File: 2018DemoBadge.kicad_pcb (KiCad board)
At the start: 2 copper layers, 8 parts, among them U1 PIC16F15325

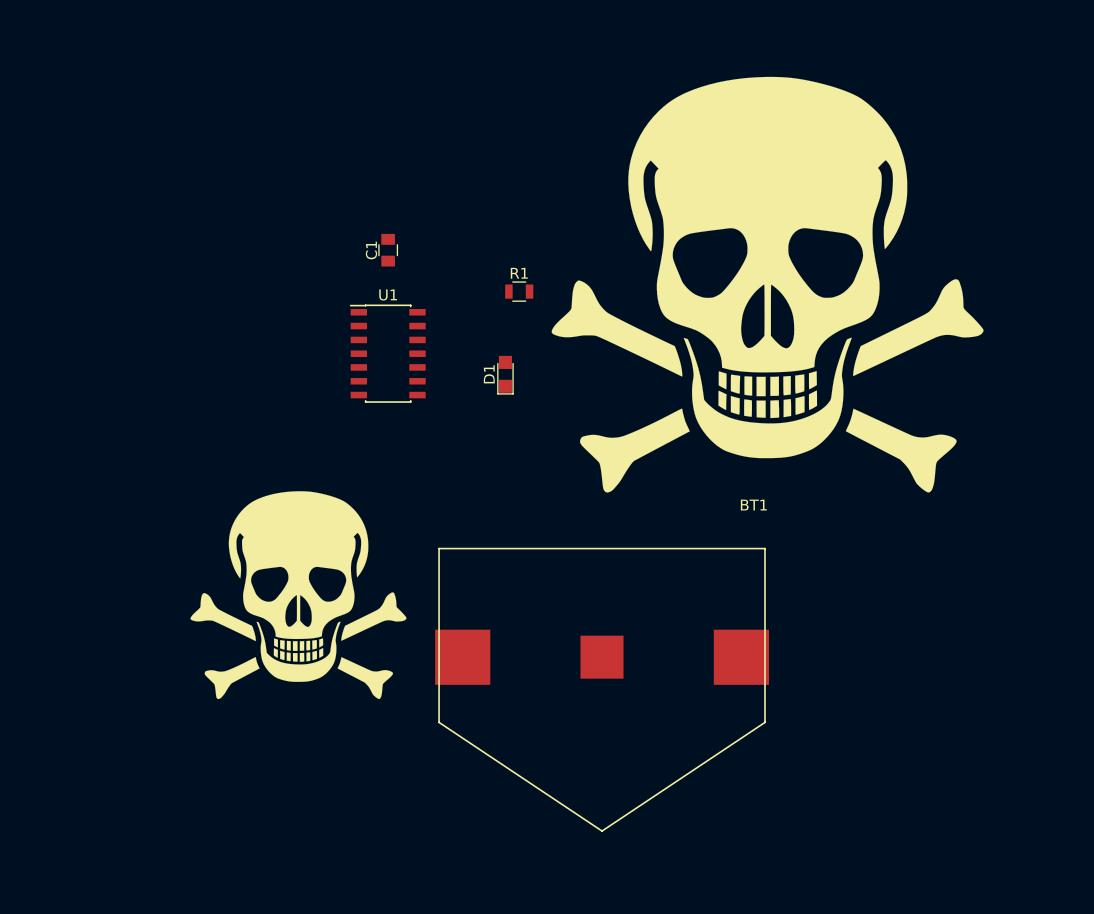
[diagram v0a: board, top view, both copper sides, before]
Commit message: skulls and copper fill zone unconnected
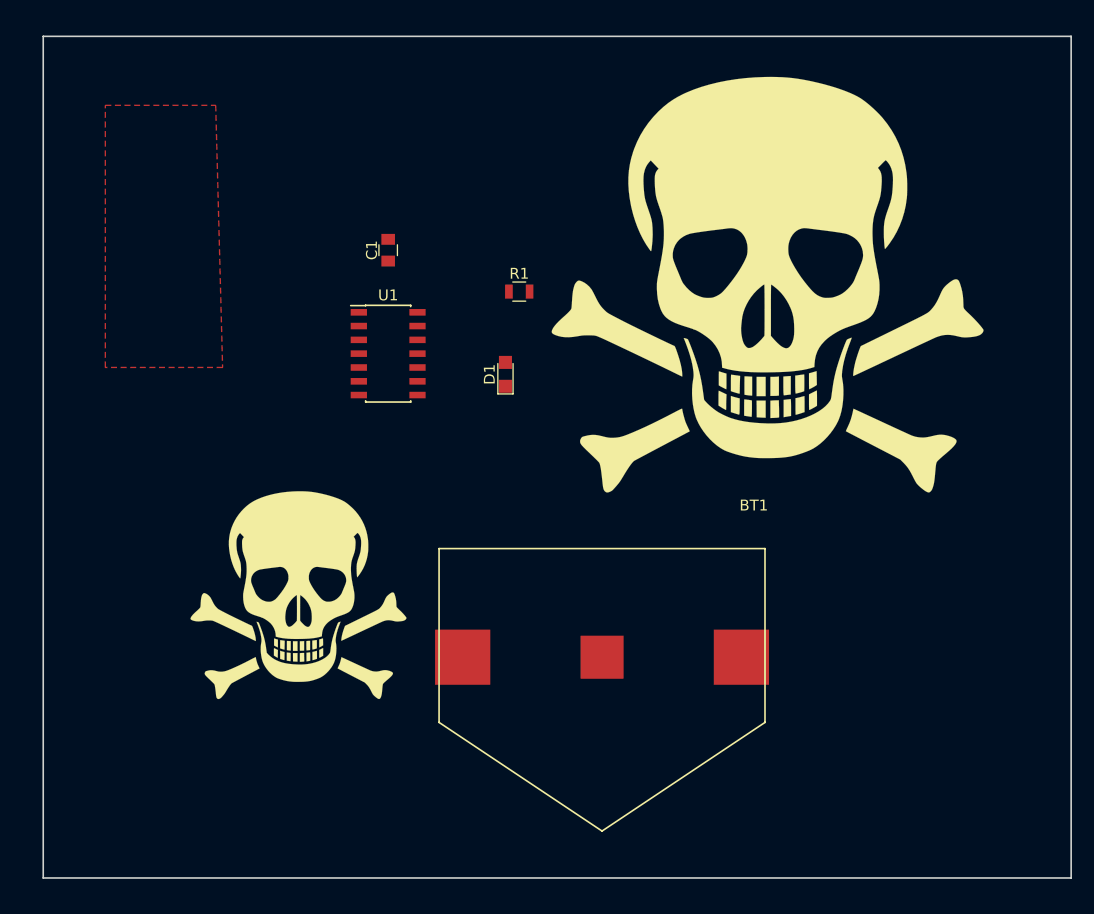
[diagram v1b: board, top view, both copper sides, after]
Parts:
- moved G*** 4.26 mm to (113.7, 87.0)
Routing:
- added copper zone on F.Cu, net (none)
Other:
- board outline added: 94.6 x 77.5 mm
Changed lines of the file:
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@@
     (links 8)
     (no_connects 8)
-    (area 105.430881 70.84252 185.181817 140.735001)
+    (area 98.349999 67.234999 193.115001 144.855001)
     (thickness 1.6)
-    (drawings 0)
+    (drawings 4)
     (tracks 0)
     (zones 0)
@@
   )
   (module FootprintLibrary:SkullCrossbones2000SM (layer F.Cu)
-    (at 115.57 83.185)
+    (at 113.665 86.995)
     (fp_text reference G*** (at 0 0) (layer F.SilkS) hide
       (effects (font (thickness 0.3)))
@@
       (xy 0.432817 -9.558067)) (layer F.Mask) (width 0.01))
   )
+  (gr_line (start 193.04 67.31) (end 98.425 67.31) (angle 90) (layer Edge.Cuts) (width 0.15))
+  (gr_line (start 193.04 144.78) (end 193.04 67.31) (angle 90) (layer Edge.Cuts) (width 0.15))
+  (gr_line (start 98.425 144.78) (end 193.04 144.78) (angle 90) (layer Edge.Cuts) (width 0.15))
+  (gr_line (start 98.425 67.31) (end 98.425 144.78) (angle 90) (layer Edge.Cuts) (width 0.15))
+  (zone (net 0) (net_name "") (layer F.Cu) (hatch edge 0.508)
+    (connect_pads (clearance 0.508))
+    (min_thickness 0.254)
+    (fill yes (arc_segments 16) (thermal_gap 0.508) (thermal_bridge_width 0.508))
+    (polygon
+      (pts
+        (xy 114.935 97.79) (xy 104.14 97.79) (xy 104.14 73.66) (xy 114.3 73.66)
+      )
+    )
+  )
 )

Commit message: skulls and copper fill zone unconnected
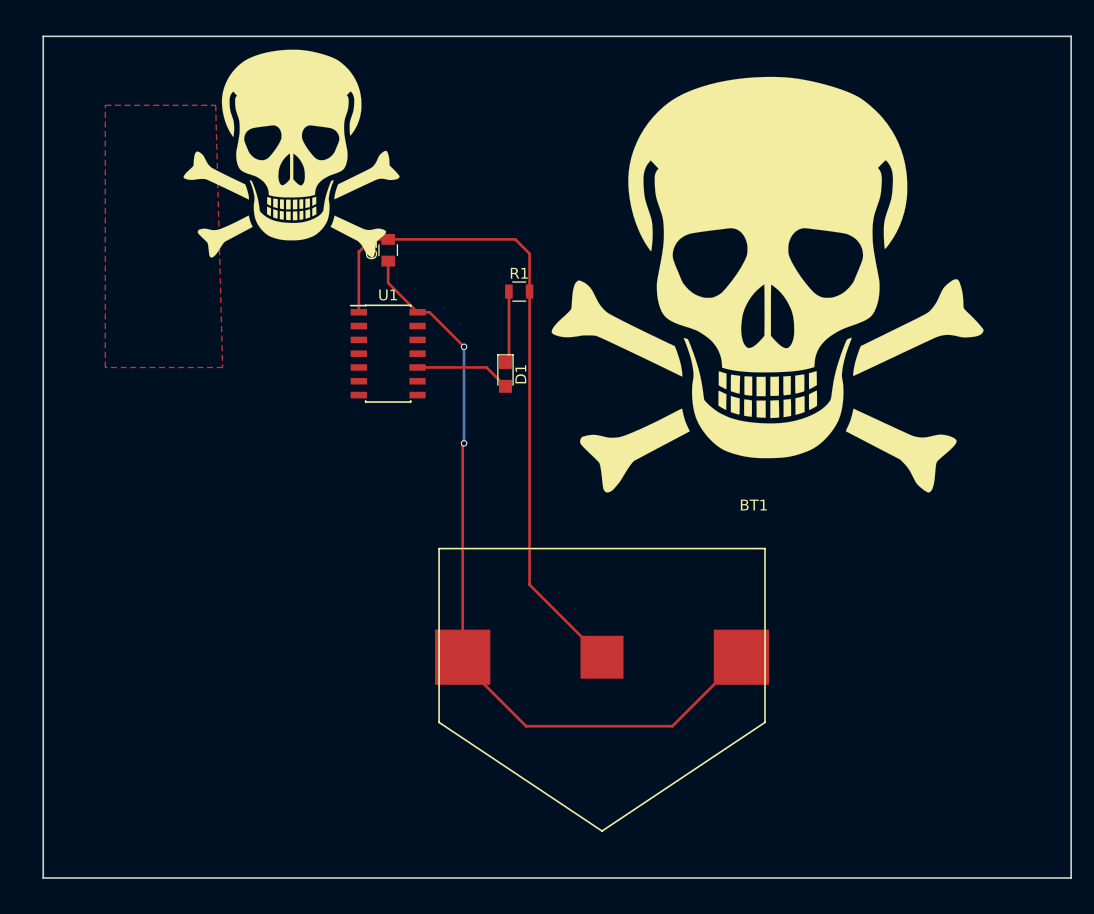
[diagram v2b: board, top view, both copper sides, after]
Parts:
- moved G*** 40.6 mm to (121.3, 78.1)
- turned D1 to 270 degrees
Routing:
- net /VSS: track 0.00 -> 71.3 mm, vias 0 -> 2
- net GND: track 0.00 -> 62.2 mm
- net Net-(D1-Pad2): track 0.00 -> 8.81 mm
- net Net-(D1-Pad1): track 0.00 -> 6.65 mm
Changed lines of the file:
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@@
   (general
     (links 8)
-    (no_connects 8)
+    (no_connects 0)
     (area 98.349999 67.234999 193.115001 144.855001)
     (thickness 1.6)
     (drawings 4)
-    (tracks 0)
+    (tracks 25)
     (zones 0)
     (modules 8)
@@
   )
   (module FootprintLibrary:LED_0805 (layer F.Cu)
-    (at 140.97 98.425 90)
+    (at 140.97 98.425 270)
     (descr "LED 0805 smd package")
     (tags "LED led 0805 SMD smd SMT smt smdled SMDLED smtled SMTLED")
     (attr smd)
-    (fp_text reference D1 (at 0 -1.45 90) (layer F.SilkS)
+    (fp_text reference D1 (at 0 -1.45 270) (layer F.SilkS)
       (effects (font (size 1 1) (thickness 0.15)))
     )
-    (fp_text value LED (at 0 1.55 90) (layer F.Fab)
+    (fp_text value LED (at 0 1.55 270) (layer F.Fab)
       (effects (font (size 1 1) (thickness 0.15)))
     )
@@
     (fp_line (start -1.95 0.85) (end -1.95 -0.85) (layer F.CrtYd) (width 0.05))
     (fp_line (start -1.95 -0.85) (end 1.95 -0.85) (layer F.CrtYd) (width 0.05))
-    (fp_text user %R (at 0 -1.25 90) (layer F.Fab)
+    (fp_text user %R (at 0 -1.25 270) (layer F.Fab)
       (effects (font (size 0.4 0.4) (thickness 0.1)))
     )
-    (pad 2 smd rect (at 1.1 0 270) (size 1.2 1.2) (layers F.Cu F.Paste F.Mask)
+    (pad 2 smd rect (at 1.1 0 90) (size 1.2 1.2) (layers F.Cu F.Paste F.Mask)
       (net 3 "Net-(D1-Pad2)"))
-    (pad 1 smd rect (at -1.1 0 270) (size 1.2 1.2) (layers F.Cu F.Paste F.Mask)
+    (pad 1 smd rect (at -1.1 0 90) (size 1.2 1.2) (layers F.Cu F.Paste F.Mask)
       (net 4 "Net-(D1-Pad1)"))
     (model ${KISYS3DMOD}/LEDs.3dshapes/LED_0805.wrl
@@
   )
   (module FootprintLibrary:SkullCrossbones2000 (layer F.Cu)
-    (at 121.92 118.745)
+    (at 121.285 78.105)
     (fp_text reference G*** (at 0 0) (layer F.SilkS) hide
       (effects (font (thickness 0.3)))
@@
   (gr_line (start 98.425 144.78) (end 193.04 144.78) (angle 90) (layer Edge.Cuts) (width 0.15))
   (gr_line (start 98.425 67.31) (end 98.425 144.78) (angle 90) (layer Edge.Cuts) (width 0.15))
+  (segment (start 143.19 90.805) (end 143.19 117.79) (width 0.25) (layer F.Cu) (net 1) (status 400000))
+  (segment (start 143.19 117.79) (end 149.86 124.46) (width 0.25) (layer F.Cu) (net 1) (status 800000))
+  (segment (start 130.175 85.995) (end 141.875 85.995) (width 0.25) (layer F.Cu) (net 1))
+  (segment (start 143.19 87.31) (end 143.19 90.805) (width 0.25) (layer F.Cu) (net 1))
+  (segment (start 141.875 85.995) (end 143.19 87.31) (width 0.25) (layer F.Cu) (net 1))
+  (segment (start 127.475 92.71) (end 127.475 87.155) (width 0.25) (layer F.Cu) (net 1))
+  (segment (start 128.635 85.995) (end 130.175 85.995) (width 0.25) (layer F.Cu) (net 1))
+  (segment (start 127.475 87.155) (end 128.635 85.995) (width 0.25) (layer F.Cu) (net 1))
+  (segment (start 137.035 124.46) (end 137.035 104.9) (width 0.25) (layer F.Cu) (net 2) (status 400000))
+  (segment (start 133.985 92.71) (end 132.875 92.71) (width 0.25) (layer F.Cu) (net 2) (status 800000))
+  (segment (start 137.16 95.885) (end 133.985 92.71) (width 0.25) (layer F.Cu) (net 2))
+  (via (at 137.16 95.885) (size 0.6) (drill 0.4) (layers F.Cu B.Cu) (net 2))
+  (segment (start 137.16 104.775) (end 137.16 95.885) (width 0.25) (layer B.Cu) (net 2))
+  (via (at 137.16 104.775) (size 0.6) (drill 0.4) (layers F.Cu B.Cu) (net 2))
+  (segment (start 137.035 104.9) (end 137.16 104.775) (width 0.25) (layer F.Cu) (net 2))
+  (segment (start 137.035 124.46) (end 137.035 124.97) (width 0.25) (layer F.Cu) (net 2) (status C00000))
+  (segment (start 137.035 124.97) (end 142.875 130.81) (width 0.25) (layer F.Cu) (net 2) (status 400000))
+  (segment (start 142.875 130.81) (end 156.335 130.81) (width 0.25) (layer F.Cu) (net 2))
+  (segment (start 156.335 130.81) (end 162.685 124.46) (width 0.25) (layer F.Cu) (net 2) (status 800000))
+  (segment (start 130.175 87.995) (end 130.175 90.01) (width 0.25) (layer F.Cu) (net 2))
+  (segment (start 130.175 90.01) (end 132.875 92.71) (width 0.25) (layer F.Cu) (net 2))
+  (segment (start 132.875 97.79) (end 139.235 97.79) (width 0.25) (layer F.Cu) (net 3) (status 400000))
+  (segment (start 139.235 97.79) (end 140.97 99.525) (width 0.25) (layer F.Cu) (net 3) (status 800000))
+  (segment (start 141.29 90.805) (end 141.29 97.005) (width 0.25) (layer F.Cu) (net 4) (status C00000))
+  (segment (start 141.29 97.005) (end 140.97 97.325) (width 0.25) (layer F.Cu) (net 4) (status C00000))
   (zone (net 0) (net_name "") (layer F.Cu) (hatch edge 0.508)
     (connect_pads (clearance 0.508))

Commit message: graphics on back - smaller badge
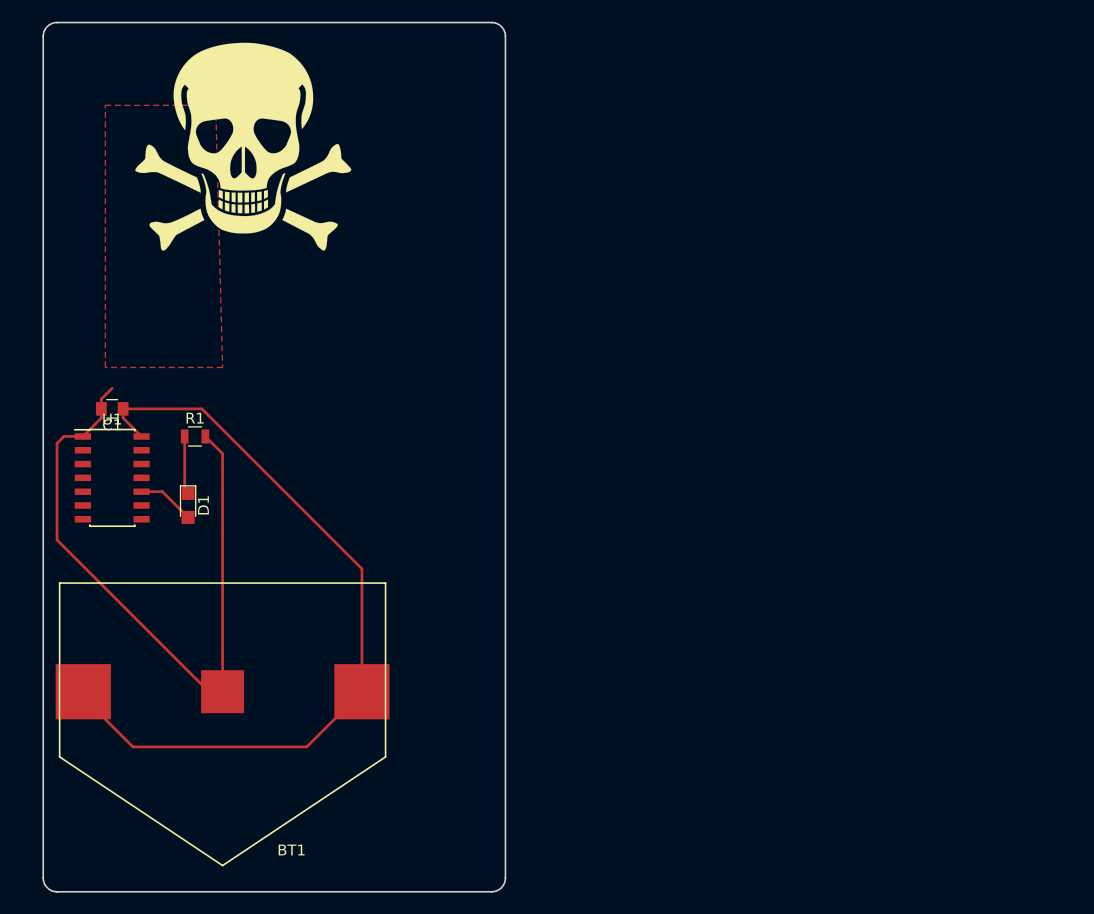
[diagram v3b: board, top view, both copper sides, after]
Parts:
- G***: moved to B.Cu
- moved G*** 57.0 mm to (120.0, 125.1), turned to 180 degrees
- moved BT1 35.1 mm to (114.9, 127.6)
- moved R1 32.7 mm to (112.4, 104.1)
- moved D1 31.6 mm to (111.8, 110.5)
- moved C1 29.3 mm to (104.8, 101.6), turned to 180 degrees
- moved U1 27.9 mm to (104.8, 108.0)
- moved G*** 4.49 mm to (116.8, 77.5)
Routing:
- net Net-(D1-Pad2): track 8.81 -> 5.27 mm
- net /VSS: track 71.3 -> 72.8 mm, vias 2 -> 0
- net Net-(D1-Pad1): track 6.65 -> 5.38 mm
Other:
- board size 94.6 x 77.5 mm -> 42.5 x 80 mm

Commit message: set for first test run of graphics
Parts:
- added G***: LOGO, FootprintLibrary:skullwallpaper, B.Cu at (116.8, 82.5)
- moved G*** 0.90 mm to (119.4, 125.7)
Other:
- board size 42.5 x 80 mm -> 45.7 x 80 mm
- net class Power added: clearance 0.2, trace_width 0.4572, via_dia 0.6, via_drill 0.4
- board text added: "Cutout"
- board text added: "MayhemBadges Testing of graphics on mask, bare board, and copper"
